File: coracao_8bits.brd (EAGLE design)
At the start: 78 x 72 mm, 73 parts, among them IC1 74HC595D, IC2 74HC595D, IC3 74HC595D, IC4 74HC595D, J1 FEMALE 2x3, J2 POWER_JACK, U2 ATMEGA168, Y1 16MHZ

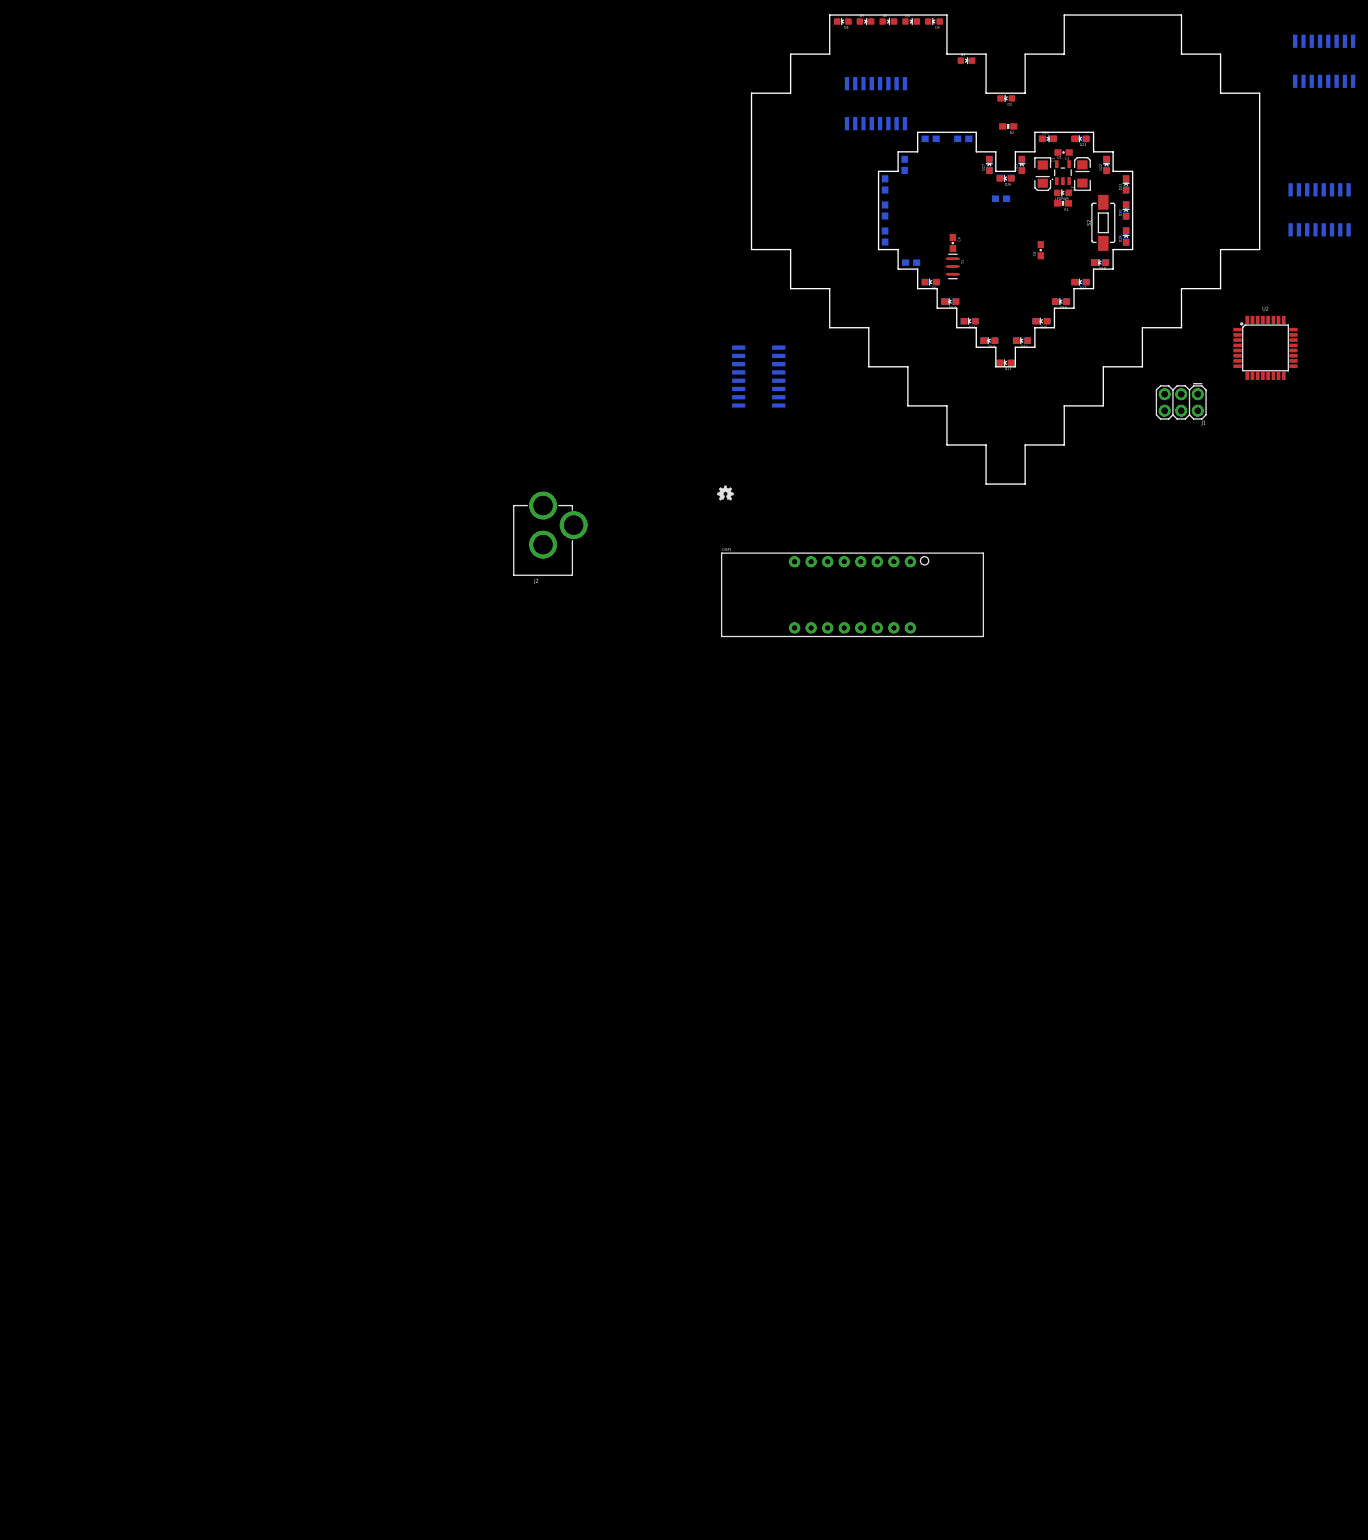
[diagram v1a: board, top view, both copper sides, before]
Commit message: adicionado mais 2 CIs e mais LEDs, total 45
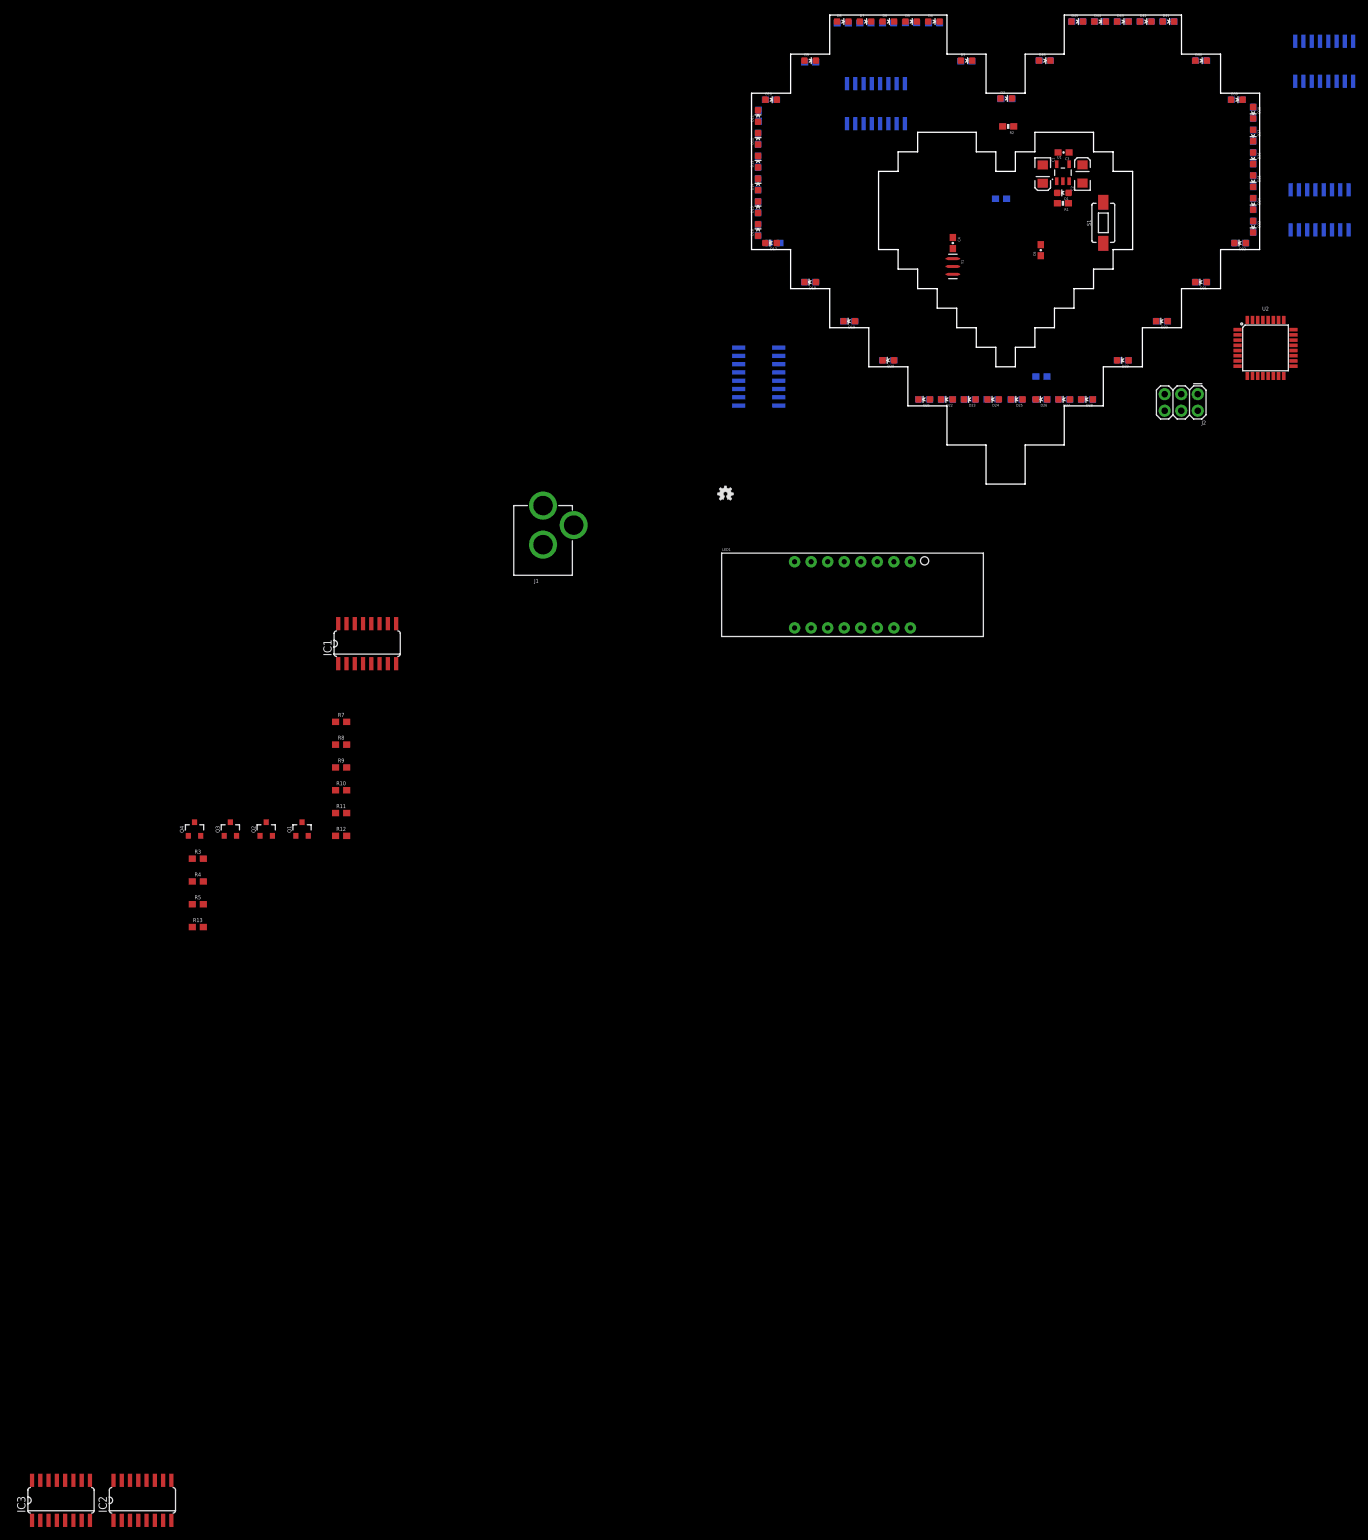
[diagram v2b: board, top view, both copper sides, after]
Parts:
- added D28, D29, D30, D31, D32, D33, D34, D35, D36, D37, D38, D39, D40, D41, D42, D43, D44, D45, D46: BLUE, SparkFun-LED:LED-0603
- added IC5, IC6, IC7: 74HC595D, 74xx-eu:SO16
- added Q1, Q2, Q3, Q4: 600mA/40V, SparkFun-DiscreteSemi:SOT23-3
- added R29, R30, R31, R32, R33, R34, R35, R36, R37, R38, R39, R40, R41, R42, R43, R44, R45, R46, R47, R48, R49, R50, R51, R52, R53, R54, R55, R56, R57, R58: 510, SparkFun-Resistors:0603-RES
- IC1: value 74HC595D -> 4511D; device 74xx-eu:SO16 -> 45xx:SO16
- J1: value FEMALE 2x3 -> POWER_JACK; device SparkFun-Connectors:2X3 -> SparkFun-Connectors:POWER_JACK_PTH
- J2: value POWER_JACK -> FEMALE 2x3; device SparkFun-Connectors:POWER_JACK_PTH -> SparkFun-Connectors:2X3
- R10, R11, R12, R13, R3, R4, R5, R6, R7, R8, R9: value 510 -> 470; device SparkFun-Resistors:0603-RES -> SparkFun-Resistors:0603
- moved IC3 276.7 mm to (-145.0, -192.0), flipped to the top
- moved IC2 196.7 mm to (-132.5, -192.0), flipped to the top, turned to 0 degrees
- moved R3 161.3 mm to (-124.0, -93.5), flipped to the top
- moved R4 160.2 mm to (-124.0, -97.0), flipped to the top, turned to 0 degrees
- moved R5 157.0 mm to (-124.0, -100.5), flipped to the top, turned to 0 degrees
- moved R13 151.2 mm to (-124.0, -104.0), flipped to the top
- moved R12 124.7 mm to (-102.0, -90.0), flipped to the top
- moved R11 122.1 mm to (-102.0, -86.5), flipped to the top
- moved R10 119.5 mm to (-102.0, -83.0), flipped to the top
- moved R9 116.9 mm to (-102.0, -79.5), flipped to the top
- moved R7 114.6 mm to (-102.0, -72.5), flipped to the top, turned to 0 degrees
- moved R8 114.3 mm to (-102.0, -76.0), flipped to the top, turned to 0 degrees
- moved IC1 113.9 mm to (-98.0, -60.5), flipped to the top, turned to 0 degrees
- moved J1 105.1 mm to (-71.0, -53.0), turned to 0 degrees
- moved J2 105.1 mm to (29.5, -22.2), turned to 180 degrees
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- renumbered DISP1 to LED1, LEDPWR to D1, S2 to S1
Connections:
- new net D28: IC7.2, R40.2
- new net D29: IC7.3, R41.2
- new net D30: IC7.4, R42.2
- new net D31: IC7.5, R43.2
- new net D32: IC7.6, R44.2
- new net D33: IC7.7, R45.2
- new net D34: IC2.15, R46.2
- new net D35: IC2.1, R47.2
- new net D36: IC2.2, R48.2
- new net D37: IC2.3, R49.2
- new net D38: IC2.4, R50.2
- new net D39: IC2.5, R51.2
- new net D40: IC2.6, R52.2
- new net D41: IC2.7, R53.2
- new net D42: IC3.15, R54.2
- new net D43: IC3.1, R55.2
- new net D44: IC3.2, R56.2
- new net D45: IC3.3, R57.2
- new net D46: IC3.4, R58.2
- new net D47: IC3.5
- new net N$104: IC5.9, IC6.14
- new net N$31: IC1.10, R9.1
- new net N$33: IC1.11, R8.1
- new net N$34: IC1.12, R7.1
- new net N$35: IC1.13, R6.1
- new net N$36: IC1.9, R10.1
- new net N$37: IC1.15, R11.1
- new net N$38: IC1.14, R12.1
- new net N$39: LED1.14, R6.2
- new net N$42: LED1.16, R7.2
- new net N$43: LED1.13, R8.2
- new net N$44: LED1.3, R9.2
- new net N$45: LED1.5, R10.2
- new net N$46: LED1.11, R11.2
- new net N$47: LED1.15, R12.2
- new net N$48: LED1.8, Q4.2
- new net N$49: LED1.6, Q3.2
- new net N$50: LED1.2, Q2.2
- new net N$51: LED1.1, Q1.2
- new net N$52: Q2.1, R4.2
- new net N$53: Q4.1, R13.2
- new net N$54: Q3.1, R5.2
- new net N$55: Q1.1, R3.2
- new net N$56: D28.A, R40.1
- new net N$57: D29.A, R41.1
- new net N$58: D30.A, R42.1
- new net N$59: D31.A, R43.1
- new net N$60: D32.A, R44.1
- new net N$61: D33.A, R45.1
- new net N$62: D34.A, R46.1
- new net N$64: D35.A, R47.1
- new net N$65: D36.A, R48.1
- new net N$66: D37.A, R49.1
- new net N$67: D38.A, R50.1
- new net N$68: D39.A, R51.1
- new net N$69: D40.A, R52.1
- new net N$70: D41.A, R53.1
- new net N$71: D42.A, R54.1
- new net N$72: D43.A, R55.1
- new net N$73: D44.A, R56.1
- new net N$74: D45.A, R57.1
- new net N$75: D46.A, R58.1
- new net OUT: IC2.14, IC7.9
- new net VDD: IC1.16
- new net VSS: IC1.8
- net D10: now also IC5.15, R22.2; no longer IC2.15, R11.2
- net D11: now also IC5.1, R23.2; no longer IC2.1, R12.2
- net D12: now also IC5.2, R24.2; no longer IC2.2, R13.2
- net D13: now also IC5.3, R25.2; no longer IC2.3, R14.2
- net D14: now also IC5.4, R26.2; no longer IC2.4, R15.2
- net D15: now also IC5.5, R27.2; no longer IC2.5, R16.2
- net D16: now also IC5.6, R28.2; no longer IC2.6, R17.2
- net D17: now also IC5.7, R29.2; no longer IC2.7, R18.2
- net D18: now also IC6.15, R30.2; no longer IC3.15, R19.2
- net D19: now also IC6.1, R31.2; no longer IC3.1, R20.2
- net D2: now also IC4.15, R14.2; no longer IC1.15, R3.2
- net D20: now also IC6.2, R32.2; no longer IC3.2, R21.2
- net D21: now also IC6.3, R33.2; no longer IC3.3, R22.2
- net D22: now also IC6.4, R34.2; no longer IC3.4, R23.2
- net D23: now also IC6.5, R35.2; no longer IC3.5, R24.2
- net D24: now also IC6.6, R36.2; no longer IC3.6, R25.2
- net D25: now also IC6.7, R37.2; no longer IC3.7, R26.2
- net D26: now also IC7.15, R38.2; no longer IC4.15, R27.2
- net D27: now also IC7.1, R39.2; no longer IC4.1, R28.2
- net D3: now also IC4.1, R15.2; no longer IC1.1, R4.2
- net D4: now also IC4.2, R16.2; no longer IC1.2, R5.2
- net D5: now also IC4.3, R17.2; no longer IC1.3, R6.2
- net D6: now also IC4.4, R18.2; no longer IC1.4, R7.2
- net D7: now also IC4.5, R19.2; no longer IC1.5, R8.2
- net D8: now also IC4.6, R20.2; no longer IC1.6, R9.2
- net D9: now also IC4.7, R21.2; no longer IC1.7, R10.2
- net DEETE: now also J1.PWR; no longer J2.PWR
- net DTR: now also J2.6; no longer J1.6
- net GND: now also D28.C, D29.C, D30.C, D31.C, D32.C, D33.C, D34.C, D35.C, D36.C, D37.C, D38.C, D39.C, D40.C, D41.C, D42.C, D43.C, D44.C, D45.C, D46.C, IC5.13, IC5.8, IC6.13, IC6.8, IC7.13, IC7.8, J1.GND, J1.GNDBREAK, J2.1; no longer IC1.13, IC1.8, J1.1, J2.GND, J2.GNDBREAK
- net LED_RCK: now also IC5.12, IC6.12, IC7.12; no longer IC1.12
- net LED_SCK: now also IC5.11, IC6.11, IC7.11; no longer IC1.11
- net LED_SERIAL: now also IC4.14; no longer IC1.14
- net N$1: now also R14.1; no longer R3.1
- net N$10: now also R23.1; no longer R12.1
- net N$11: now also R24.1; no longer R13.1
- net N$12: now also R25.1; no longer R14.1
- net N$13: now also R26.1; no longer R15.1
- net N$14: now also R27.1; no longer R16.1
- net N$15: now also R28.1; no longer R17.1
- net N$16: now also R29.1; no longer R18.1
- net N$17: now also R30.1; no longer R19.1
- net N$18: now also R31.1; no longer R20.1
- net N$19: now also R32.1; no longer R21.1
- net N$2: now also R15.1; no longer R4.1
- net N$20: now also R33.1; no longer R22.1
- net N$21: now also R34.1; no longer R23.1
- net N$22: now also R35.1; no longer R24.1
- net N$23: now also R36.1; no longer R25.1
- net N$24: now also R37.1; no longer R26.1
- net N$25: now also R38.1; no longer R27.1
- net N$26: now also R39.1; no longer R28.1
- net N$3: now also R16.1; no longer R5.1
- net N$4: now also R17.1; no longer R6.1
- net N$40: now also IC4.9, IC5.14; no longer IC1.9, IC2.14
- net N$41: now also IC6.9, IC7.14; no longer IC3.9, IC4.14
- net N$5: now also R18.1; no longer R7.1
- net N$6: now also R19.1; no longer R8.1
- net N$7: now also R20.1; no longer R9.1
- net N$8: now also R21.1; no longer R10.1
- net N$9: now also R22.1; no longer R11.1
- net RX: now also J2.3; no longer J1.3
- net TX: now also J2.4; no longer J1.4
- net VCC: now also IC5.10, IC5.16, IC6.10, IC6.16, IC7.10, IC7.16, J2.2; no longer IC1.10, IC1.16, J1.2

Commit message: finalizada
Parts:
- J1: value POWER_JACK -> (none); device SparkFun-Connectors:POWER_JACK_PTH -> SparkFun-Connectors:1X02
- moved IC3 269.9 mm to (17.5, 23.5), flipped to the bottom
- moved IC2 259.1 mm to (28.5, 11.0), flipped to the bottom, turned to 90 degrees
- moved R13 166.9 mm to (5.63, 1.12), flipped to the bottom, turned to 90 degrees
- moved Q4 161.3 mm to (9.39, 0.99), flipped to the bottom, turned to 180 degrees
- moved R5 159.7 mm to (-0.76, 1.11), flipped to the bottom, turned to 90 degrees
- moved R4 152.3 mm to (-7.50, 1.13), flipped to the bottom, turned to 90 degrees
- moved Q3 151.9 mm to (3.36, 0.94), flipped to the bottom, turned to 180 degrees
- moved R11 145.9 mm to (4.35, 13.3), flipped to the bottom, turned to 90 degrees
- moved R3 145.1 mm to (-14.0, 1.11), flipped to the bottom, turned to 90 degrees
- moved Q2 141.8 mm to (-3.84, 0.95), flipped to the bottom, turned to 180 degrees
- moved R12 141.2 mm to (-5.82, 13.4), flipped to the bottom, turned to 90 degrees
- moved R10 138.4 mm to (1.73, 8.66), flipped to the bottom, turned to 270 degrees
- moved R8 135.0 mm to (-0.77, 13.3), flipped to the bottom, turned to 90 degrees
- moved Q1 133.1 mm to (-9.93, 0.96), flipped to the bottom, turned to 180 degrees
- moved IC1 132.4 mm to (20.5, -1.50), flipped to the bottom
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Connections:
- removed net D47: IC3.5
- new net BCD_A: IC1.7, U2.23
- new net BCD_B: IC1.1, U2.24
- new net BCD_C: IC1.2, U2.25
- new net BCD_D: IC1.6, U2.26
- new net DISP_D1: R3.1, U2.27
- new net DISP_D2: R4.1, U2.28
- new net DISP_D3: R5.1, U2.19
- new net DISP_D4: R13.1, U2.22
- net DEETE: now also J1.2; no longer J1.PWR
- net GND: now also IC1.5, J1.1; no longer J1.GND, J1.GNDBREAK
- net VCC: now also IC1.3, IC1.4, Q1.3, Q2.3, Q3.3, Q4.3
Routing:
- net GND: track 0.00 -> 495.7 mm, vias 0 -> 7
- net VCC: track 0.00 -> 302.2 mm, vias 0 -> 19
- net LED_SCK: track 0.00 -> 187.0 mm, vias 0 -> 8
- net LED_RCK: track 0.00 -> 148.5 mm, vias 0 -> 7
- net N$34: track 0.00 -> 61.2 mm
- net DEETE: track 0.00 -> 53.1 mm, vias 0 -> 3
- net N$38: track 0.00 -> 47.3 mm
- net LED_SERIAL: track 0.00 -> 43.0 mm, vias 0 -> 1
- net DTR: track 0.00 -> 36.6 mm, vias 0 -> 2
- net OUT: track 0.00 -> 33.9 mm
- net N$104: track 0.00 -> 31.8 mm, vias 0 -> 2
- net DISP_D1: track 0.00 -> 31.4 mm, vias 0 -> 1
- net N$33: track 0.00 -> 31.0 mm
- net D33: track 0.00 -> 30.7 mm, vias 0 -> 2
- net N$35: track 0.00 -> 29.3 mm, vias 0 -> 2
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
